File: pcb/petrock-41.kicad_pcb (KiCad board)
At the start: 2 copper layers, 242.5 x 87.9 mm, 102 parts, among them J1 MJ-4PP-9, J2 OLED, J3 MJ-4PP-9, J4 OLED, SW1 SW_PUSH, SW10 SW_PUSH, SW11 SW_PUSH, SW12 SW_PUSH, SW13 SW_PUSH, SW14 SW_PUSH, SW15 SW_PUSH, SW16 SW_PUSH, SW17 SW_PUSH, SW18 SW_PUSH, SW19 SW_PUSH, SW2 SW_PUSH, SW20 SW_PUSH, SW21 SW_PUSH, SW22 SW_PUSH, SW23 SW_PUSH, SW24 SW_PUSH, SW25 SW_PUSH, SW26 SW_PUSH, SW27 SW_PUSH, SW29 SW_PUSH, SW3 SW_PUSH, SW30 SW_PUSH, SW31 SW_PUSH, SW32 SW_PUSH, SW33 SW_PUSH, SW34 SW_PUSH, SW35 SW_PUSH, SW36 SW_PUSH, SW37 SW_PUSH, SW38 SW_PUSH, SW39 SW_PUSH, SW4 SW_PUSH, SW41 SW_PUSH, SW42 SW_PUSH, SW43 SW_PUSH, SW44 SW_PUSH, SW5 SW_PUSH, SW6 SW_PUSH, SW8 SW_PUSH, SW9 SW_PUSH, U1 ProMicro, U2 ProMicro

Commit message: Standoffs in a rectangle, screw holes back in the switch plate
The standoff stack is holykeebs': a spacer through the main board's 3.1 mm
hole, a top screw through the switch plate, a bottom screw through the
bottom plate; the main board hangs from the switches. The plate's screw
holes, removed early on as supposed OLED-cover holes, are back (2.1 mm)
over every standoff.

Per half, four standoffs sit at four-key centres forming a 54 x 34 mm
rectangle (pinky|ring and index|inner index, top and bottom) and one at
the thumbs. The logo's standoff moves to the index bottom, so the logo
carries a solid 7 mm dot on board and plate. README: hardware (5 mm round
spacers; small-head top screws where four keys meet), assembly and feet.
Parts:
- moved h2 32.0 mm to (107.5, 107.2)
- moved h2 32.0 mm to (204.2, 107.2)
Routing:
- net col0_r: track 32.6 -> 99.8 mm, vias 2 -> 6
- net VCC: track 64.6 -> 87.5 mm, vias 2 -> 4
- net GND: track 475.0 -> 496.3 mm, vias 10 -> 13
- net VDD: track 128.3 -> 108.2 mm, vias 7 -> 8
- net col2: track 162.0 -> 145.8 mm, vias 9 -> 7
- net col0: track 165.1 -> 155.4 mm, vias 11 -> 7
- net col3_r: track 128.4 -> 132.6 mm, vias 3 -> 5
- net col1_r: track 175.1 -> 177.4 mm
- net col1: track 172.9 -> 171.2 mm, vias 6 -> 10
- net row3: track 157.4 -> 156.0 mm
- net row3_r: track 157.7 -> 158.9 mm
- net GNDA: track 482.4 -> 483.4 mm
- net col4_r: track 139.0 -> 138.2 mm, vias 5 -> 6
- net TP_CLK: track 66.8 -> 67.3 mm

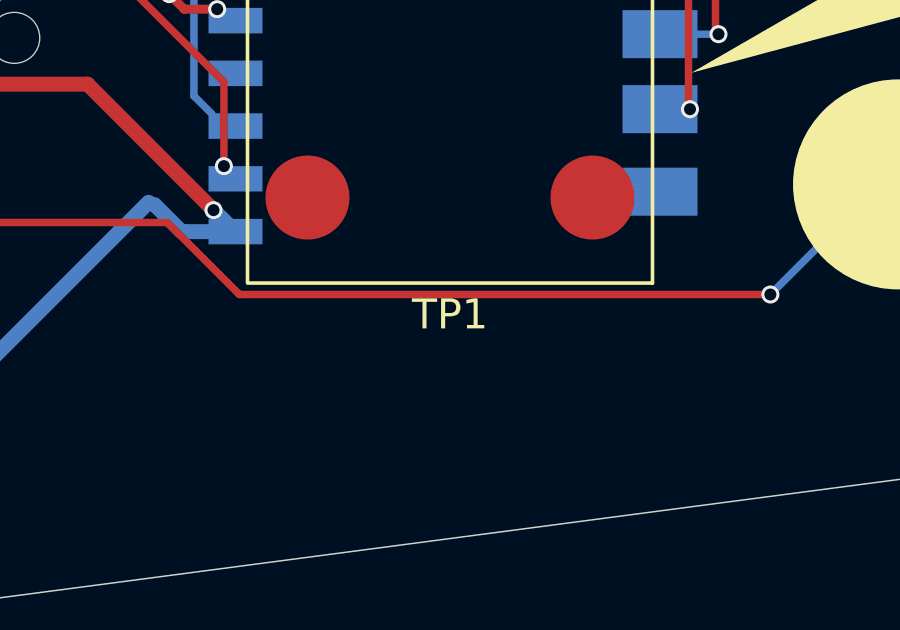
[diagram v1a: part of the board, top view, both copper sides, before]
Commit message: Jack pads masked tight, version stamp, A1-A4 for the trackpoint parts
The stock jack footprint's solder-mask openings showed bare ground beside
the supply pad, where a hand-soldered bridge would short it: the jack pads'
mask opening now matches the pad (no solder-mask bridges left; DRC has no
errors). holykeebs' revision stamp gives way to ours (name, version,
repository) on the back between the controller's pin rows. The trackpoint
sensor and controller boards become A1-A4 (assemblies), not TP (test point).
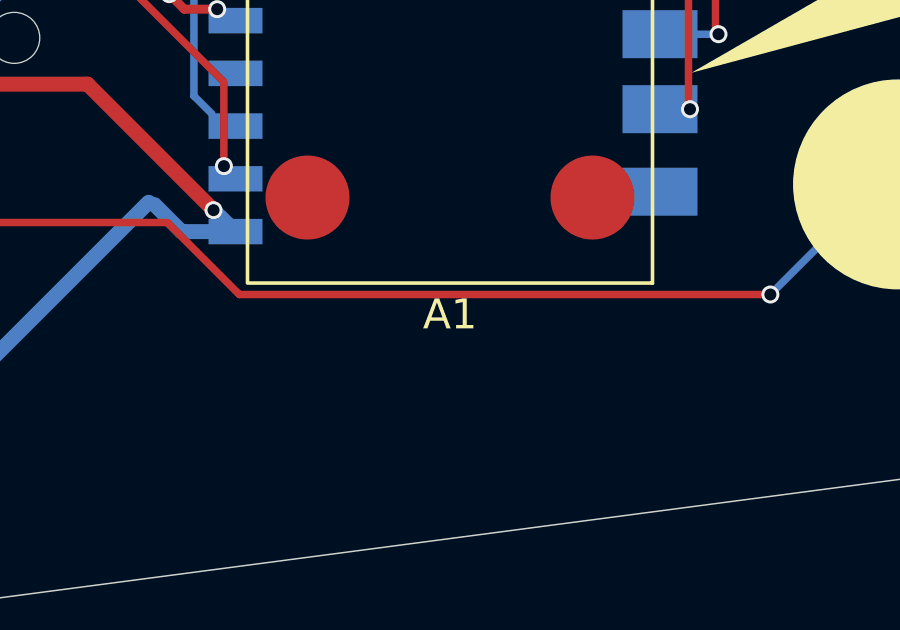
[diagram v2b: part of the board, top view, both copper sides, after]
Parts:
- renumbered TP1 to A1, TP2 to A2
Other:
- board text added: "PETROCK-41 v3.10"
- board text added: "github.com/dycli/petrock"
- board text removed: "271364f"

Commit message: Boards, plates and renders built from 06b7685 (the hash printed on the boards)
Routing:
- net col0: track 155.4 -> 203.5 mm, vias 7 -> 17
- net col0_r: track 99.8 -> 130.9 mm, vias 6 -> 9
- net VCC: track 87.5 -> 64.6 mm, vias 4 -> 2
- net GND: track 496.3 -> 475.0 mm, vias 13 -> 10
- net col1_r: track 177.4 -> 192.8 mm, vias 4 -> 8
- net col2: track 145.8 -> 143.2 mm, vias 7 -> 5
- net row3_r: track 158.9 -> 157.7 mm
- net VDD: track 108.2 -> 109.4 mm, vias 8 -> 9
- net col1: track 171.2 -> 170.3 mm, vias 10 -> 6
- net row2: track 132.8 -> 133.5 mm, vias 6 -> 8
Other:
- board text added: "06b7685"
- board text removed: "PETROCK-41 v3.10"
- board text removed: "github.com/dycli/petrock"

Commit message: Boards, plates and renders built from b9e0fd4 (the hash printed on the boards)
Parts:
- moved D15 8.83 mm to (55.9, 93.9)
- moved D13 8.69 mm to (55.9, 110.9)
- moved D9 8.56 mm to (55.9, 76.9)
- moved D1 8.39 mm to (37.9, 113.2)
- moved D10 8.34 mm to (73.9, 74.5)
- moved D3 7.59 mm to (55.9, 59.9)
- moved D14 5.29 mm to (37.9, 96.2)
- moved D29 3.76 mm to (260.6, 79.2)
- moved D35 2.16 mm to (260.6, 96.2)
- moved D19 2.06 mm to (87.6, 112.7)
- moved D22 2.04 mm to (260.6, 113.2)
- moved D21 1.67 mm to (128.7, 120.0), turned to 60 degrees
- moved D45 1.67 mm to (137.2, 105.3), turned to 60 degrees
- moved D20 1.67 mm to (108.6, 113.6), turned to 75 degrees
- moved D23 1.55 mm to (260.6, 62.2)
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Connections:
- SW41 pad 1: col4_r -> col3_r
- SW42 pad 1: col5_r -> col4_r
- SW44 pad 1: col0_r -> col5_r
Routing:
- net GNDA: track 483.4 -> 4.31 mm, vias 5 -> 107
- net GND: track 475.0 -> 2.54 mm, vias 10 -> 146
- net col0: track 203.5 -> 53.9 mm, vias 17 -> 0
- net col0_r: track 130.9 -> 0.00 mm, vias 9 -> 0
- net VDD: track 109.4 -> 201.0 mm, vias 9 -> 1
- net col3_r: track 133.0 -> 209.7 mm, vias 5 -> 2
- net TP_DATA: track 68.2 -> 127.7 mm
- net TP_CLK: track 67.3 -> 124.7 mm
- net reset: track 63.8 -> 36.2 mm, vias 1 -> 0
- net VCC: track 64.6 -> 91.3 mm, vias 2 -> 1
- net row2_r: track 91.8 -> 116.3 mm
- net reset_r: track 42.9 -> 19.2 mm
- net col1: track 170.3 -> 147.2 mm, vias 6 -> 2
- net col4_r: track 138.1 -> 161.0 mm, vias 6 -> 2
- net col2: track 143.2 -> 125.0 mm, vias 5 -> 2
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- added copper zone on F.Cu, net GND
- added copper zone on F.Cu, net GNDA
- removed copper zone on F.Cu, net (none)
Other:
- board text added: "b9e0fd4"
- board text removed: "06b7685"
